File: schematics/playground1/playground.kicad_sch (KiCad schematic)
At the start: 44 parts, among them SW1 SW_SPST, U1 ADS1299, U2 TLV75533PDBV, U3 AP2112K-5.0

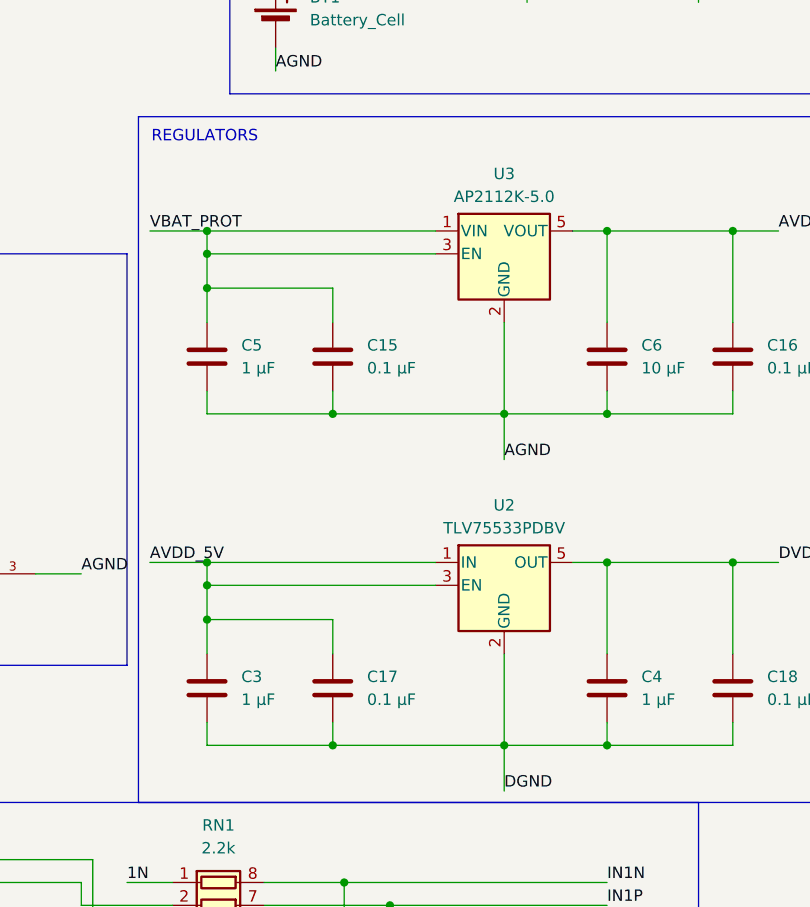
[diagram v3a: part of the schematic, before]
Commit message: update voltage regulators to ones we can buy
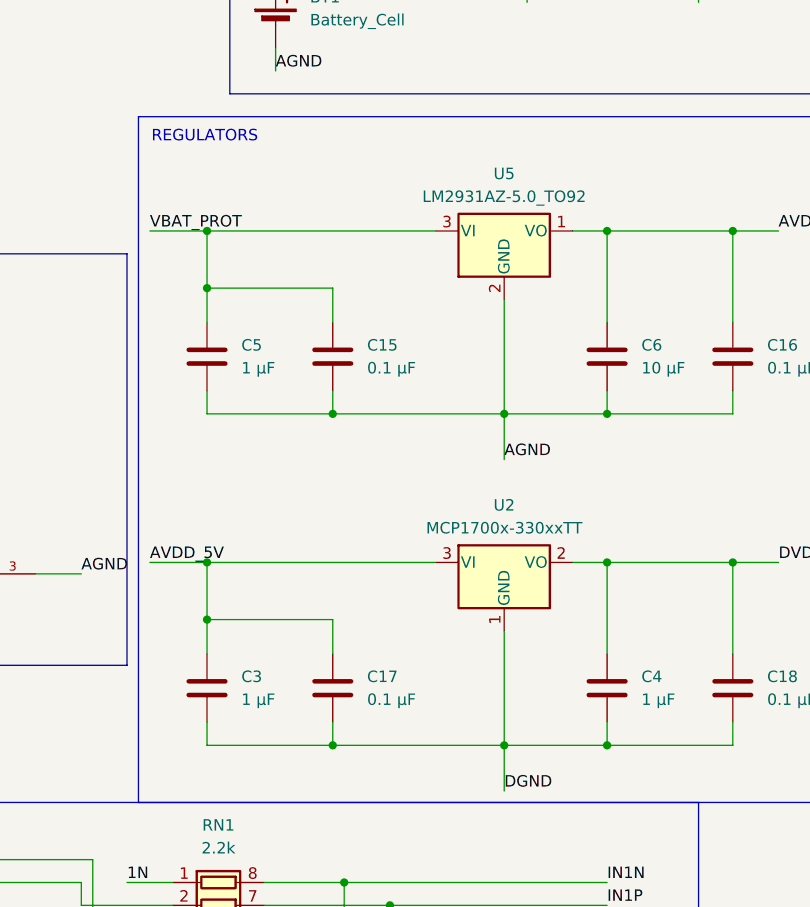
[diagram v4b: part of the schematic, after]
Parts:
- removed U2: TLV75533PDBV, Package_TO_SOT_SMD:SOT-23-5, symbol Regulator_Linear:TLV75533PDBV
- removed U3: AP2112K-5.0, Package_TO_SOT_SMD:SOT-23-5, symbol Regulator_Linear:AP2112K-3.3
- added U2: MCP1700x-330xxTT, Package_TO_SOT_SMD:SOT-23, symbol Regulator_Linear:MCP1700x-330xxTT
- added U5: LM2931AZ-5.0_TO92, Package_TO_SOT_THT:TO-92_Inline, symbol Regulator_Linear:LM2931AZ-5.0_TO92
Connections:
- net AGND: now also U5.2 (GND)
- net AVDD_5V: now also U2.3 (VI), U5.1 (VO)
- net DGND: now also U2.1 (GND)
- net DVDD_3V3: now also U2.2 (VO)
- net VBAT_PROT: now also U5.3 (VI)

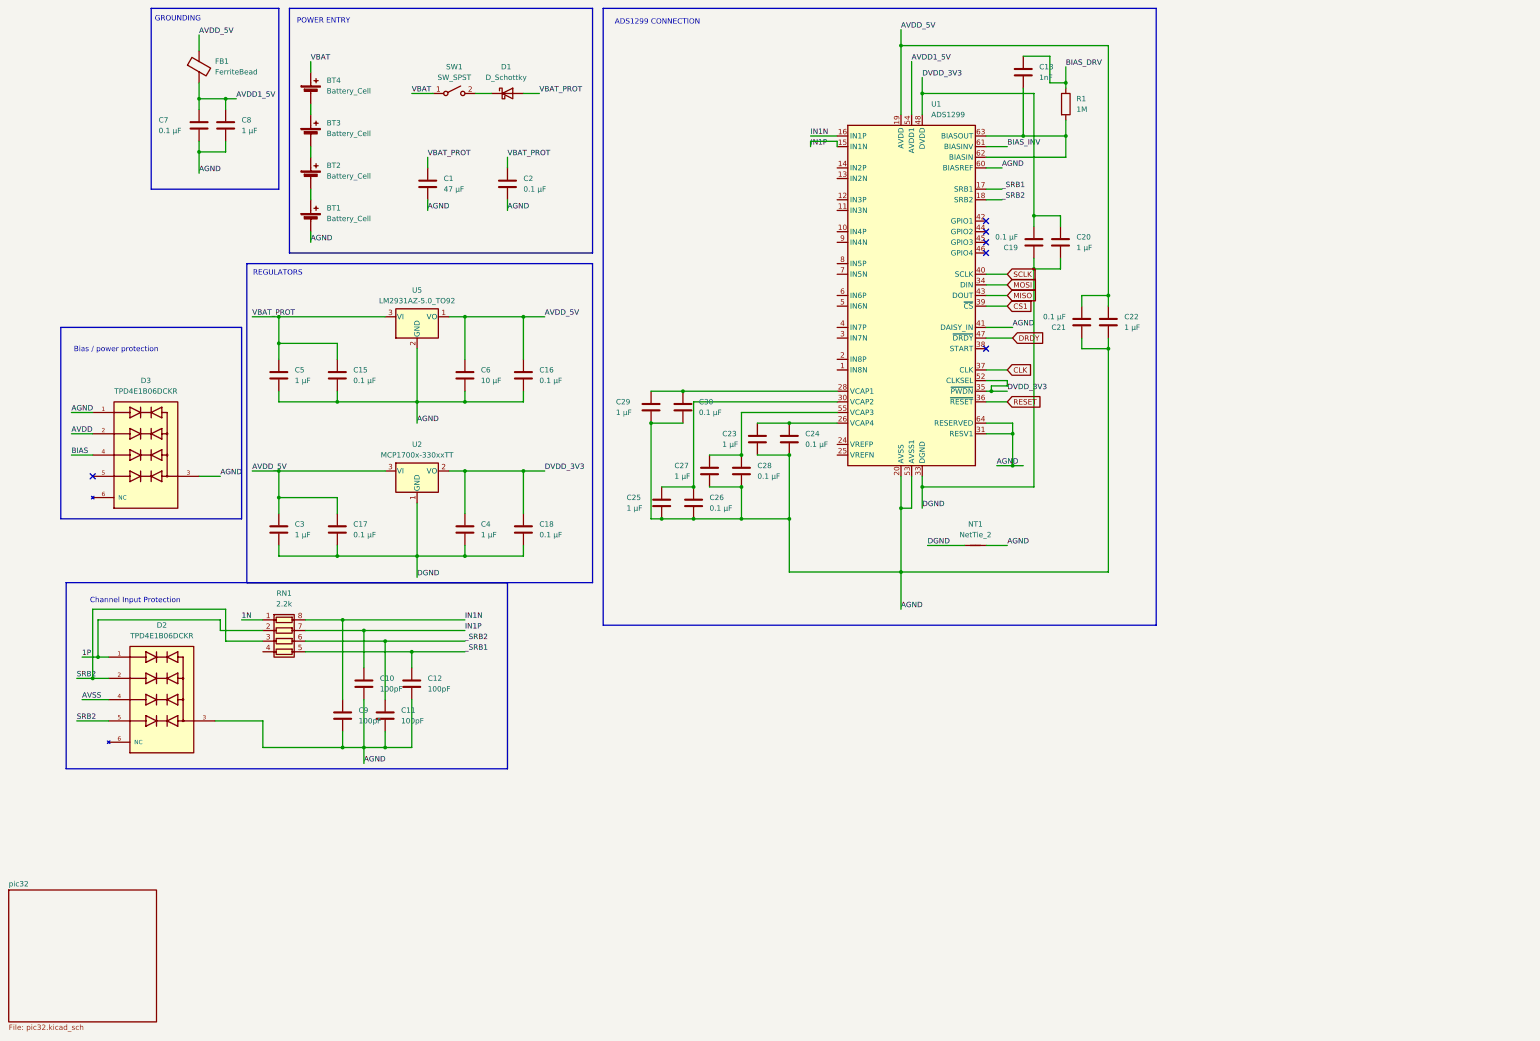
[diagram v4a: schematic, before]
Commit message: consolidate schematics into one file
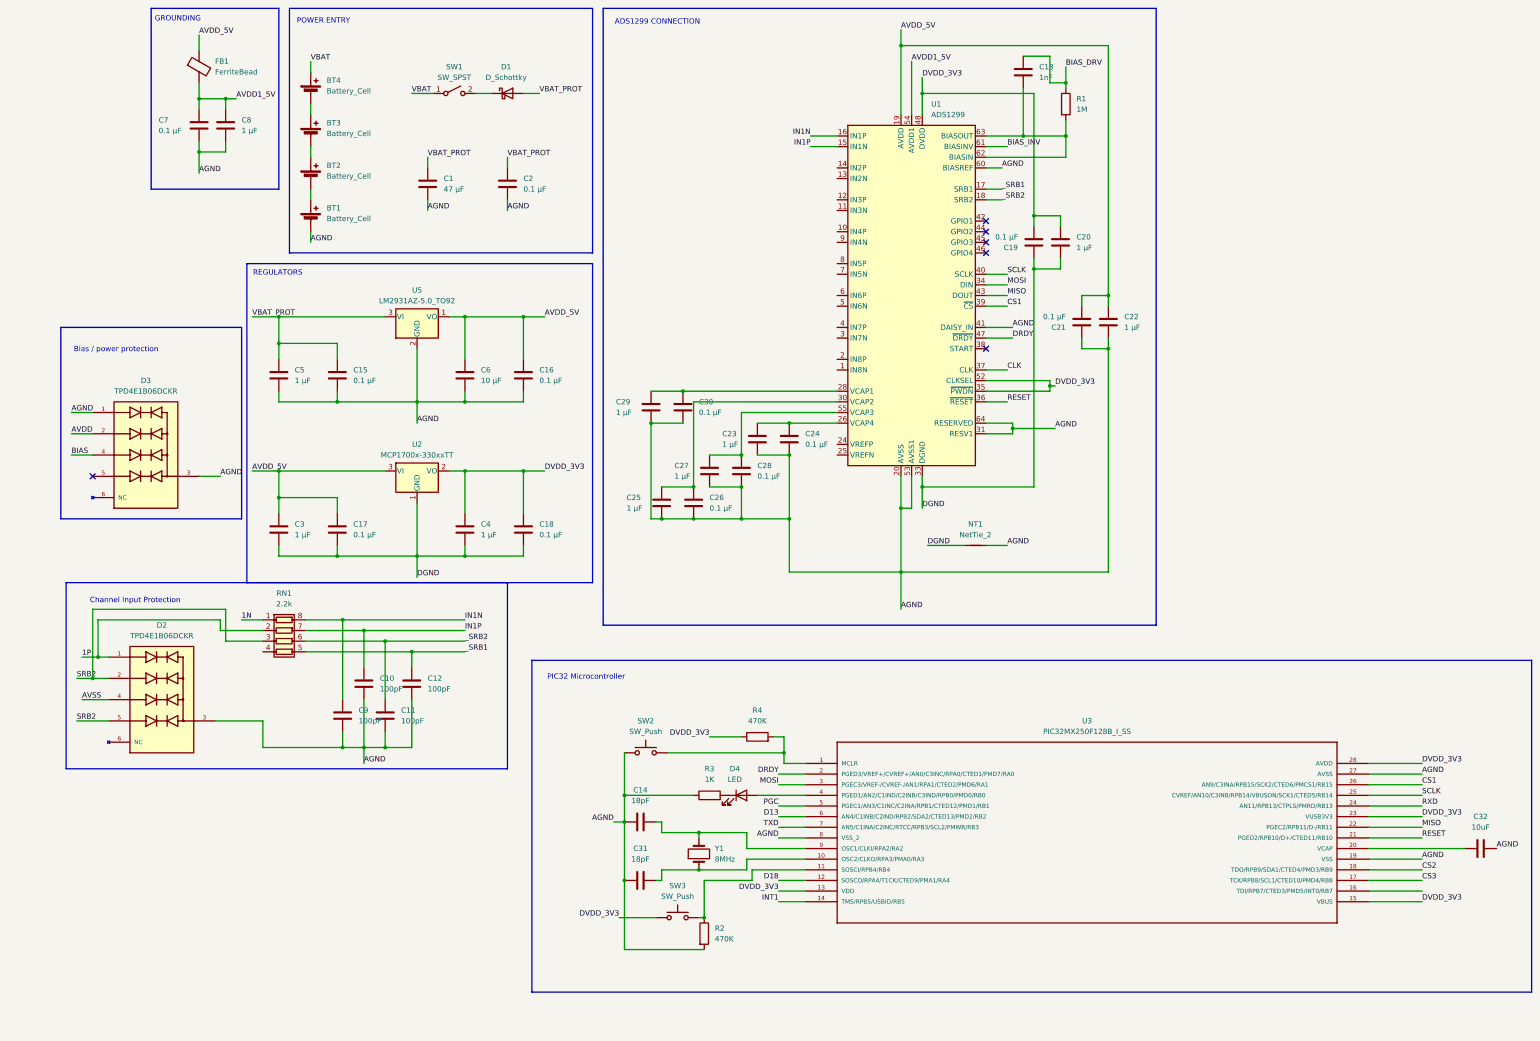
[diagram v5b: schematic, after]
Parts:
- added C14, C31: 18pF, symbol Device:C
- added C32: 10uF, symbol Device:C
- added D4: LED, symbol Device:LED
- added R2, R4: 470K, symbol Device:R
- added R3: 1K, symbol Device:R
- added SW2, SW3: SW_Push, symbol Switch:SW_Push
- added U3: PIC32MX250F128B_I_SS, PIC32MX250F128B_I_SS:SSOP28_MC, symbol PIC32MX250F128B_I_SS:PIC32MX250F128B_I_SS
- added Y1: 8MHz, symbol Device:Crystal
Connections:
- net AGND: now also C14.1, C31.2, C32.2, R2.2, R3.1, SW2.1, U3.19 (VSS), U3.27 (AVSS), U3.8 (VSS_2)
- net CS1: now also U3.26 (AN9/C3INA/RPB15/SCK2/CTED6/PMCS1/RB15)
- net DRDY: now also U3.2 (PGED3/VREF+/CVREF+/AN0/C3INC/RPA0/CTED1/PMD7/RA0)
- net DVDD_3V3: now also R4.1, SW3.1, U3.13 (VDD), U3.15 (VBUS), U3.23 (VUSB3V3), U3.28 (AVDD)
- net MISO: now also U3.22 (PGEC2/RPB11/D-/RB11)
- net MOSI: now also U3.3 (PGEC3/VREF-/CVREF-/AN1/RPA1/CTED2/PMD6/RA1)
- net RESET: now also U3.21 (PGED2/RPB10/D+/CTED11/RB10)
- net SCLK: now also U3.25 (CVREF/AN10/C3INB/RPB14/VBUSON/SCK1/CTED5/RB14)
- new net: D4.1 (K), R3.2
- new net: D4.2 (A), U3.4 (PGED1/AN2/C1IND/C2INB/C3IND/RPB0/PMD0/RB0)
- new net: R2.1, SW3.2, U3.11 (SOSCI/RPB4/RB4)
- new net: C14.2, U3.9 (OSC1/CLKI/RPA2/RA2), Y1.2
- new net: R4.2, SW2.2, U3.1 (MCLR)
- new net: C31.1, U3.10 (OSC2/CLKO/RPA3/PMA0/RA3), Y1.1
- new net: C32.1, U3.20 (VCAP)
- new net CS2: U3.18 (TDO/RPB9/SDA1/CTED4/PMD3/RB9)
- new net CS3: U3.17 (TCK/RPB8/SCL1/CTED10/PMD4/RB8)
- new net D13: U3.6 (AN4/C1INB/C2IND/RPB2/SDA2/CTED13/PMD2/RB2)
- new net D18: U3.12 (SOSCO/RPA4/T1CK/CTED9/PMA1/RA4)
- new net INT1: U3.14 (TMS/RPB5/USBID/RB5)
- new net PGC: U3.5 (PGEC1/AN3/C1INC/C2INA/RPB1/CTED12/PMD1/RB1)
- new net RXD: U3.24 (AN11/RPB13/CTPLS/PMRD/RB13)
- new net TXD: U3.7 (AN5/C1INA/C2INC/RTCC/RPB3/SCL2/PMWR/RB3)
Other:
- removed sheet pic32
- note added: "PIC32 Microcontroller"

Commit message: fix some errors
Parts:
- C6: footprint (none) -> Capacitor_Tantalum_SMD:CP_EIA-3216-18_Kemet-A_HandSolder
- R4: value 470K -> 10k
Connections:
- net 1N is gone; now on net IN1N: RN1.1 (R1.1)
- net 1P is gone; now on net IN1P: D2.1, RN1.2 (R2.1)
- net AVDD is gone; now on net AVDD_5V: D3.2
- net AVSS is gone; now on net AGND: D2.4
- net BIAS is gone; now on net BIAS_DRV: D3.4
- net AGND: now also C6.1; no longer C6.2
- net AVDD1_5V: now also FB1.1; no longer FB1.2
- net AVDD_5V: now also C6.2, FB1.2; no longer C6.1, FB1.1
- net DRDY: no longer U3.2 (PGED3/VREF+/CVREF+/AN0/C3INC/RPA0/CTED1/PMD7/RA0)
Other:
- note added: "BIAS / POWER PROTECTION"
- note added: "CHANNEL INPUT PROTECTION"
- note added: "PIC32 MICROCONTROLLER"
- note removed: "Bias / power protection"
- note removed: "Channel Input Protection"
- note removed: "PIC32 Microcontroller"
- moved on the sheet: BT1, BT2, BT3, BT4, C1, C10, C11, C12, C13, C14, C15, C16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

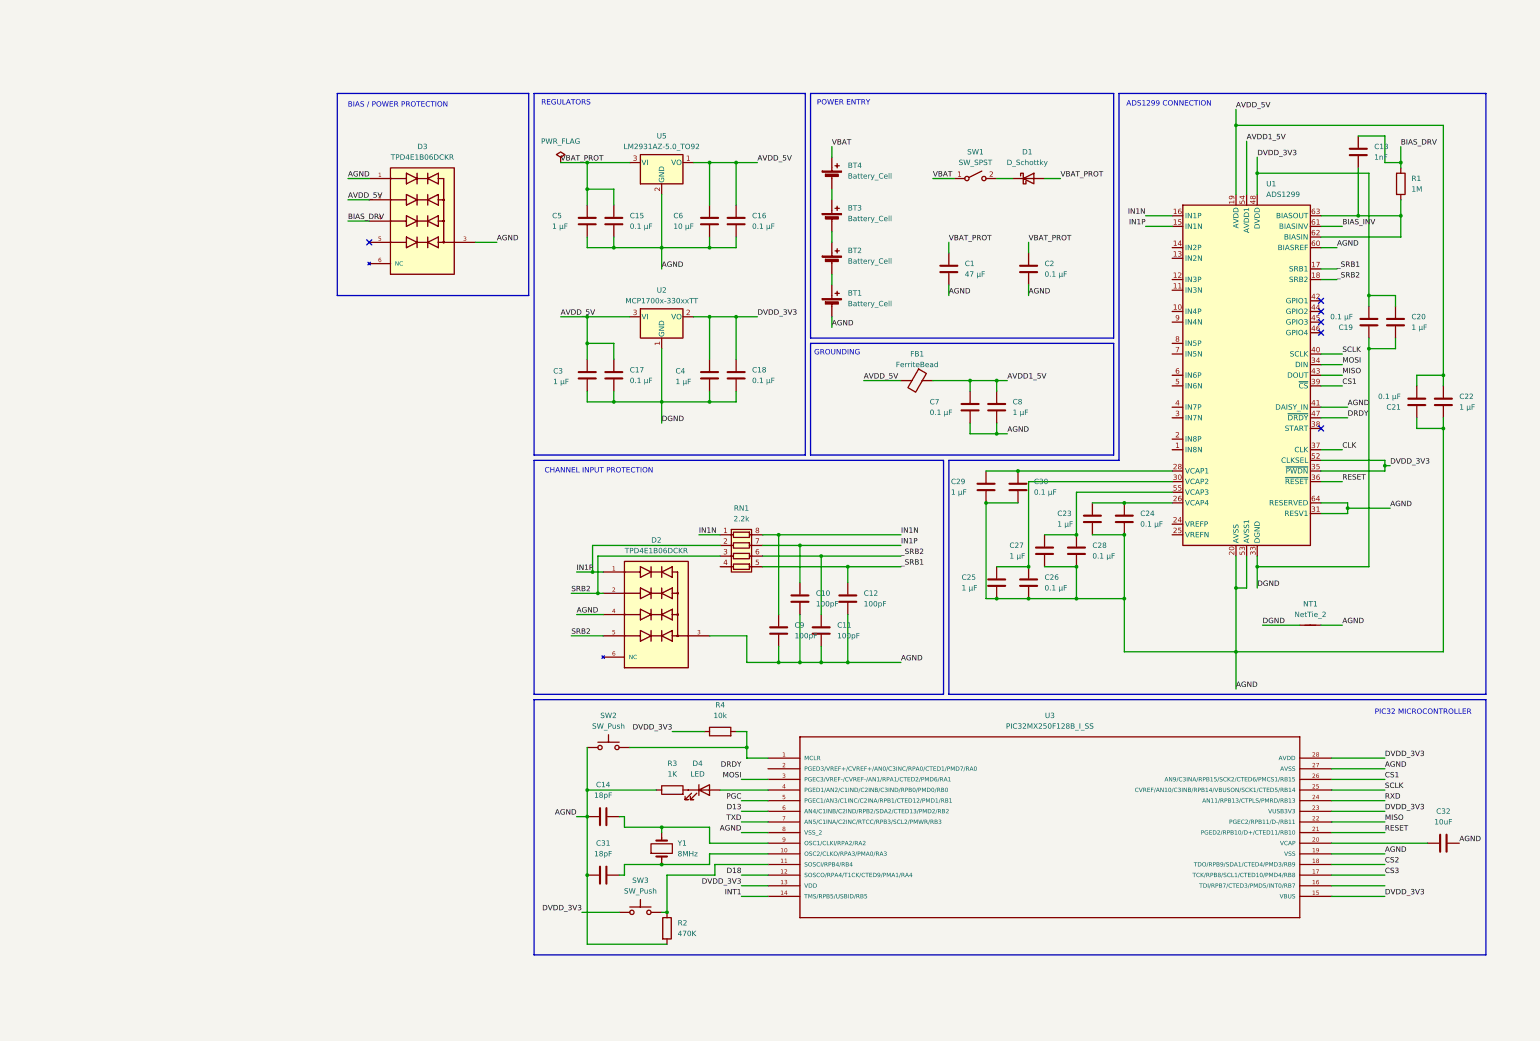
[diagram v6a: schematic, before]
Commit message: fixed label not connected ERC errors
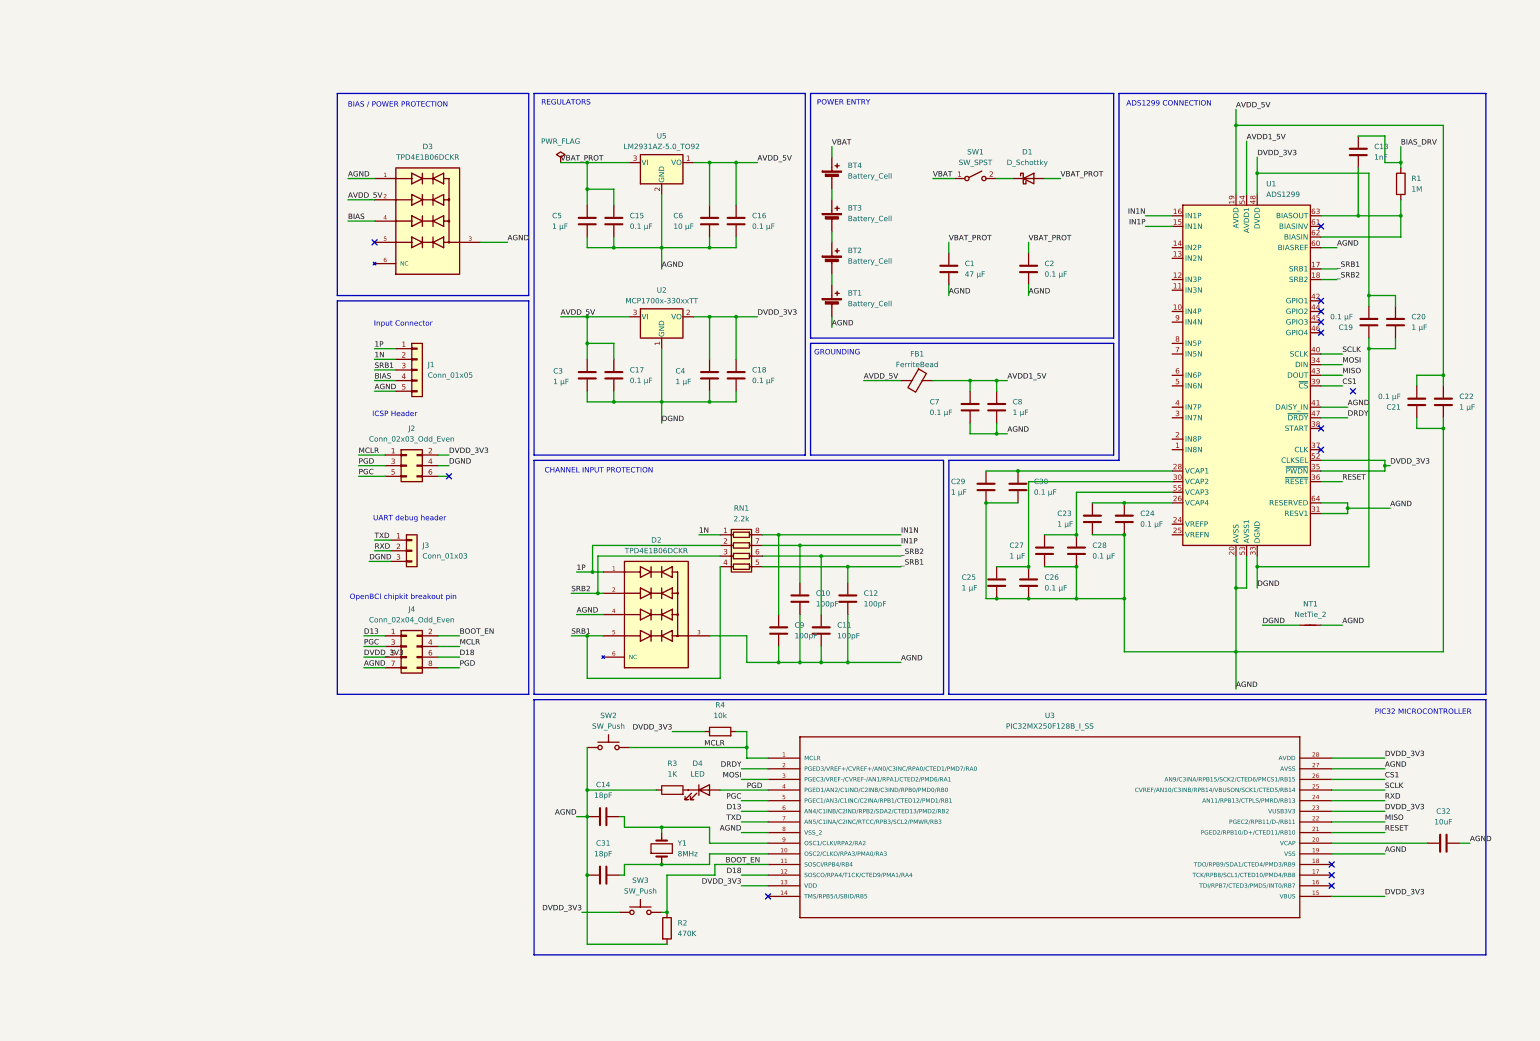
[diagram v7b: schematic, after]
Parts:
- added J1: Conn_01x05, symbol Connector_Generic:Conn_01x05
- added J2: Conn_02x03_Odd_Even, symbol Connector_Generic:Conn_02x03_Odd_Even
- added J3: Conn_01x03, symbol Connector_Generic:Conn_01x03
- added J4: Conn_02x04_Odd_Even, symbol Connector_Generic:Conn_02x04_Odd_Even
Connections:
- net AGND: now also J1.5 (Pin_5), J4.7 (Pin_7)
- net BIAS_DRV: no longer D3.4
- net D13: now also J4.1 (Pin_1)
- net D18: now also J4.6 (Pin_6)
- net DGND: now also J2.4 (Pin_4), J3.3 (Pin_3)
- net DRDY: now also U3.2 (PGED3/VREF+/CVREF+/AN0/C3INC/RPA0/CTED1/PMD7/RA0)
- net DVDD_3V3: now also J2.2 (Pin_2), J4.5 (Pin_5)
- net IN1N: no longer RN1.1 (R1.1)
- net IN1P: no longer D2.1, RN1.2 (R2.1)
- net PGC: now also J2.5 (Pin_5), J4.3 (Pin_3)
- net RXD: now also J3.2 (Pin_2)
- net SRB2: no longer D2.5
- net TXD: now also J3.1 (Pin_1)
- net PGD: now reaches D4.2 (A), U3.4 (PGED1/AN2/C1IND/C2INB/C3IND/RPB0/PMD0/RB0)
- net PGD: now also J2.3 (Pin_3), J4.8 (Pin_8)
- net BOOT_EN: now reaches R2.1, SW3.2, U3.11 (SOSCI/RPB4/RB4)
- net BOOT_EN: now also J4.2 (Pin_2)
- net MCLR: now reaches R4.2, SW2.2, U3.1 (MCLR)
- net MCLR: now also J2.1 (Pin_1), J4.4 (Pin_4)
- net SRB1: now reaches RN1.4 (R4.1)
- net SRB1: now also D2.5, J1.3 (Pin_3)
- net BIAS_INV: no longer names the net of U1.61 (BIASINV)
- net CLK: no longer names the net of U1.37 (CLK)
- net CS2: no longer names the net of U3.18 (TDO/RPB9/SDA1/CTED4/PMD3/RB9)
- net CS3: no longer names the net of U3.17 (TCK/RPB8/SCL1/CTED10/PMD4/RB8)
- net INT1: no longer names the net of U3.14 (TMS/RPB5/USBID/RB5)
- new net 1N: J1.2 (Pin_2), RN1.1 (R1.1)
- new net 1P: D2.1, J1.1 (Pin_1), RN1.2 (R2.1)
- new net BIAS: D3.4, J1.4 (Pin_4)
- no-connect marks 6 -> 14
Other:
- note added: "ICSP Header"
- note added: "Input Connector"
- note added: "OpenBCI chipkit breakout pin"
- note added: "UART debug header"
- moved on the sheet: D3

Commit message: fixed remaining pin/power errors
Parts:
- added C33: 10uF, symbol Device:C
- added C34: .1uF, symbol Device:C
- D2, D3: footprint TPD4E1B06DCKR:TVS_TPD4E1B06DCKR -> Package_TO_SOT_SMD:SOT-363_SC-70-6
- U3: footprint PIC32MX250F128B_I_SS:SSOP28_MC -> Package_SO:SSOP-28_5.3x10.2mm_P0.65mm
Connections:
- net AGND: now also U1.25 (VREFN), C33.2, C34.1
- net at U1.24 (VREFP): now also C33.1, C34.2
- no-connect marks 14 -> 27
